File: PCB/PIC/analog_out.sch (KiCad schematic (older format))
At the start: 27 parts, among them J19 TB_1X2, Q1 PBSS5240XF, Q14 BC817-40, U18 LM358, U21 MCP6022

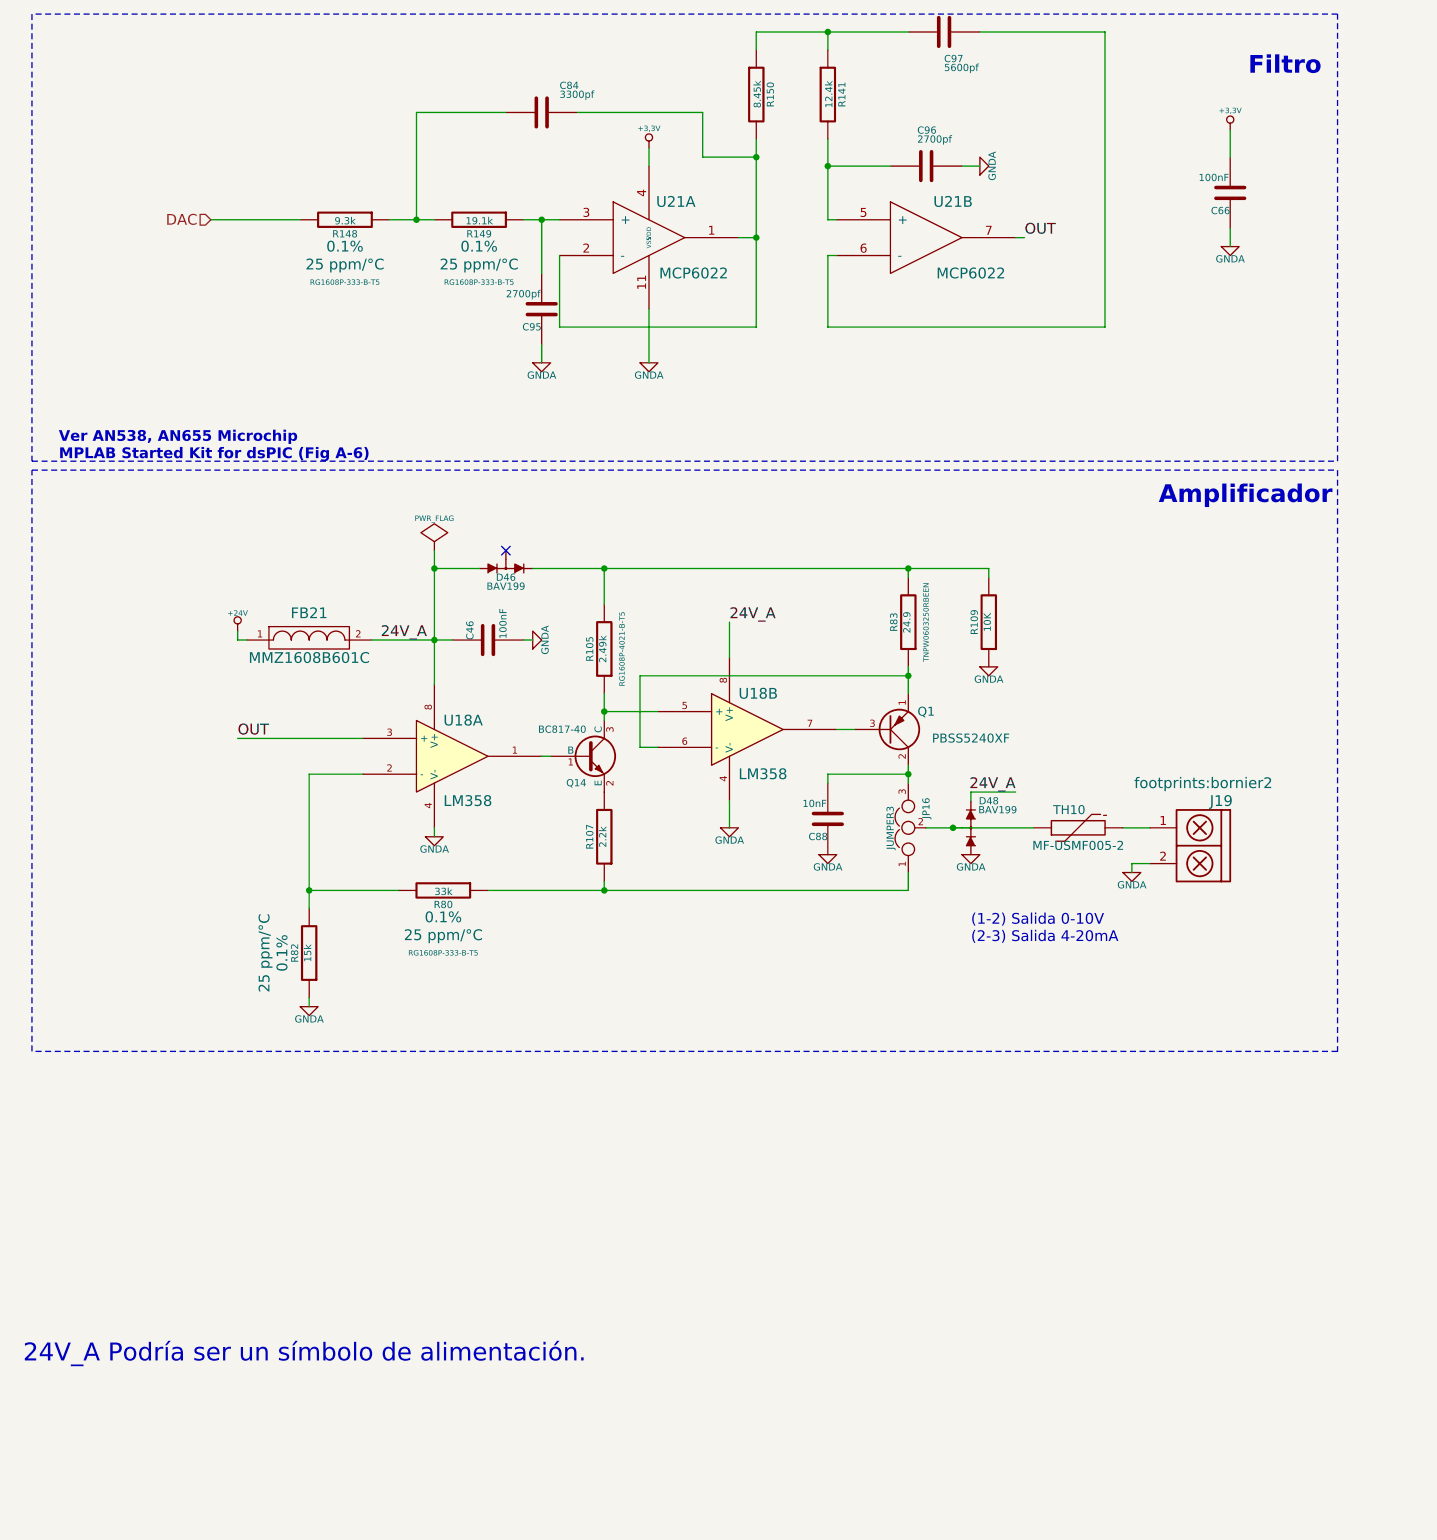
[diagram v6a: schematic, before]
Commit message: rev02 se completa campo num. de frabicante(manf#) CIAA-PIC
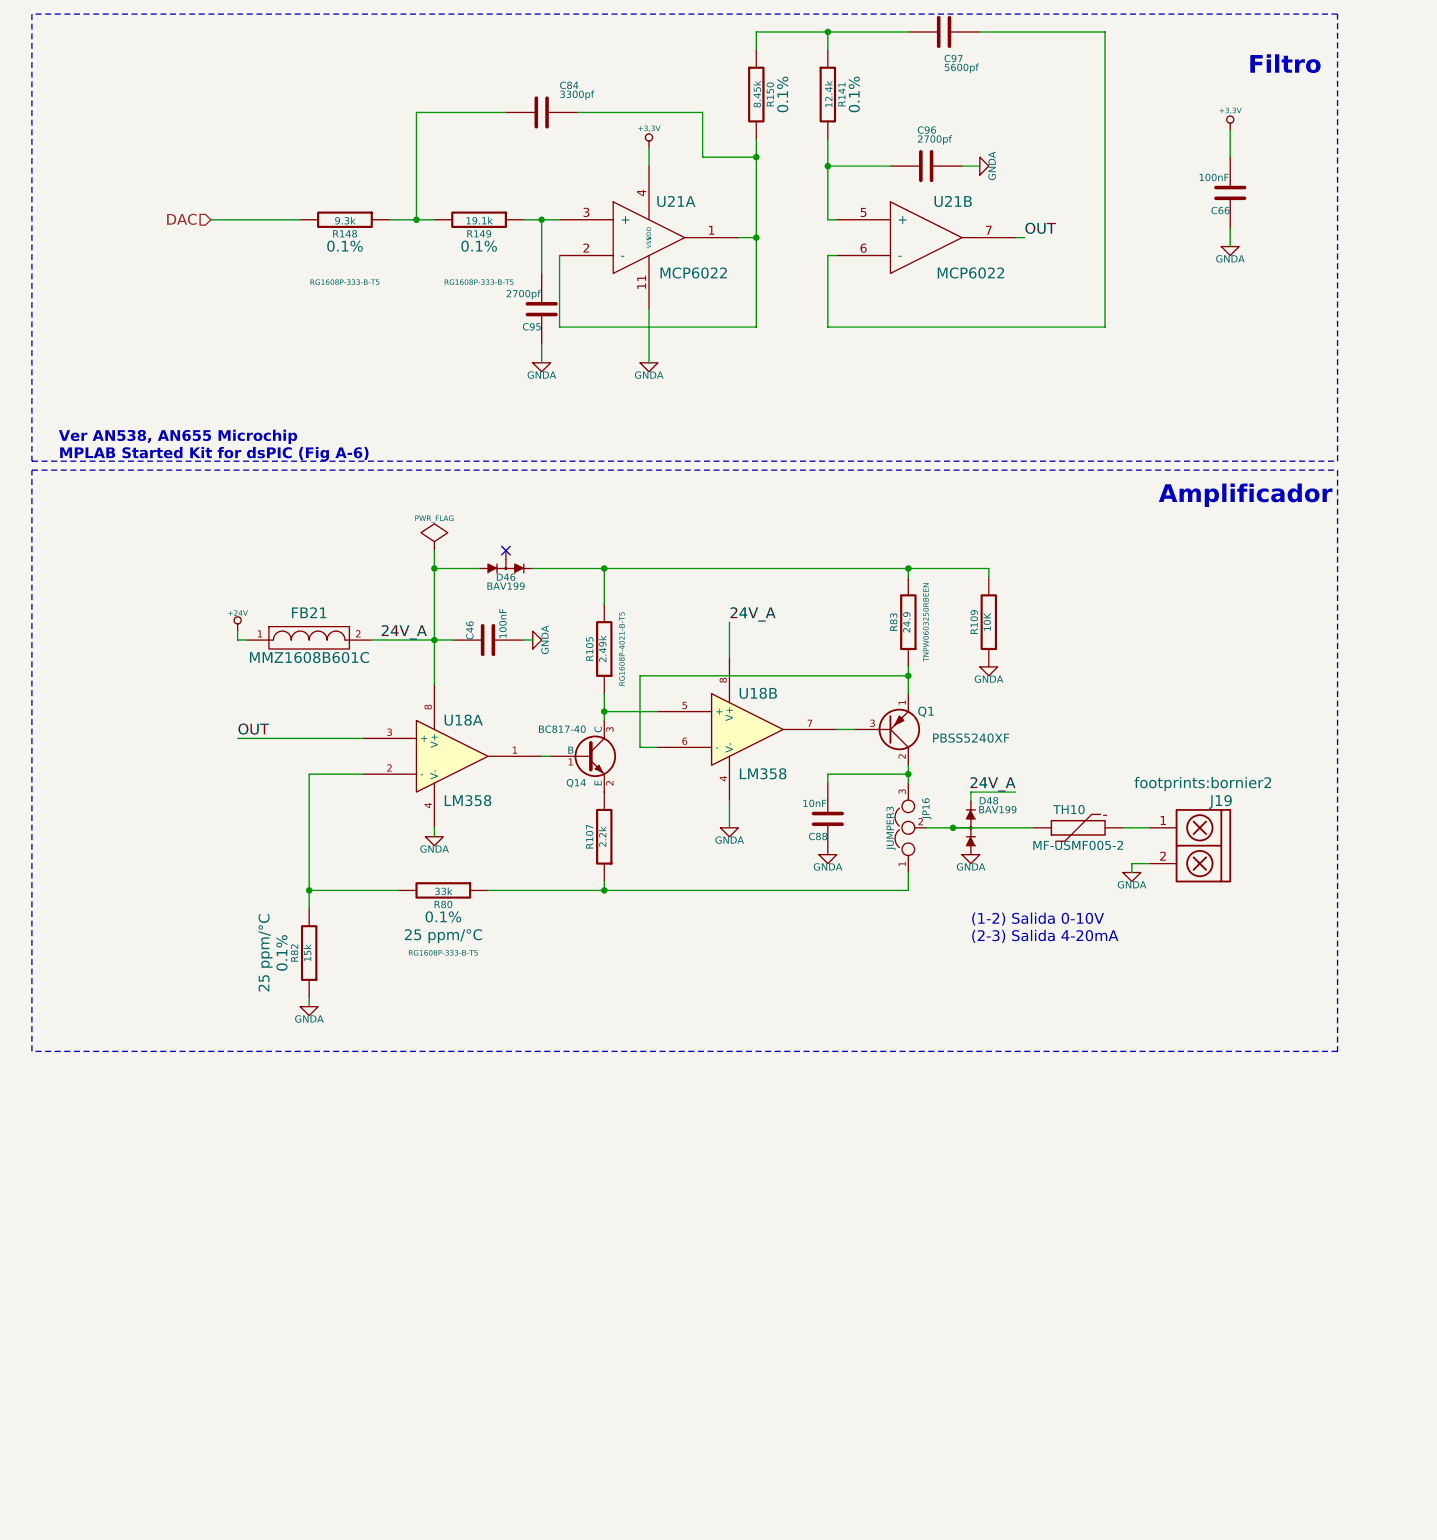
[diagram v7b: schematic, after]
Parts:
- C46, C66: #manf C0603C104K5RACTU -> (none); manf# (none) -> C0603C104K5RACTU
- C84: manf# (none) -> GRM033R71E331KA01D
- C88: #manf C0603C103K5RACTU -> (none); manf# (none) -> C0603C103K5RACTU
- C95, C96: manf# (none) -> CL10B272KB8SFNC
- C97: manf# (none) -> CL10B562KB8SFNC
- D46, D48: #manf BAV199LT1G -> (none); manf# (none) -> BAV199LT1G
- FB21: #manf MMZ1608B601CTAH0 -> (none); manf# (none) -> MMZ1608B601CTAH0
- J19: #manf OSTTC022162 -> (none); manf# (none) -> OSTTC022162
- Q1: #manf PBSS5240XF -> (none); manf# (none) -> PBSS5240XF
- Q14: #manf BC817-40LT3G -> (none); manf# (none) -> BC817-40LT3G
- R105, R83: #manf ERA-3AEB2491V -> (none); manf# (none) -> ERA-3AEB2491V
- R107: #manf ERJ-8GEYJ222V -> (none); manf# (none) -> ERJ-8GEYJ222V
- R109: #manf RC0603JR-0710KL -> (none); manf# (none) -> RC0603JR-0710KL
- R141: manf# (none) -> RC0603FR-0712K4L; tol (none) -> 0.1%
- R148: TC 25 ppm/°C -> (none); manf# (none) -> RC0603FR-079K31L
- R149: TC 25 ppm/°C -> (none); manf# (none) -> RC0603FR-0719K1L
- R150: manf# (none) -> ERJ-3EKF8451V; tol (none) -> 0.1%
- R80: #manf ERA-3AEB333V -> (none); manf# (none) -> ERA-3AEB333V
- R82: #manf RG1608P-153-B-T5 -> (none); manf# (none) -> RG1608P-153-B-T5
- TH10: #manf MF-USMF005-2 -> (none); manf# (none) -> MF-USMF005-2
- U18: #manf LM358DG -> (none); manf# (none) -> LM358DG
- U21: footprint (none) -> footprints:-SOIC8; manf# (none) -> MCP6022T-I/SN
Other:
- note removed: "24V_A Podría ser un símbolo de alimentación."
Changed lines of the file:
@@
 F 2 "Capacitors_SMD:C_0603" H 5038 4050 30  0001 C CNN
 F 3 "~" H 5000 4200 60  0000 C CNN
-F 4 "C0603C104K5RACTU" H 5000 4200 60  0001 C CNN "#manf"
+F 4 "C0603C104K5RACTU" H 5000 4200 60  0001 C CNN "manf#"
 	1    5000 4200
 	0    -1   -1   0
@@
 F 4 "0.1%" V 4900 5600 60  0000 C CNN "Tol"
 F 5 "25 ppm/°C" V 5000 5600 60  0000 C CNN "TC"
-F 6 "ERA-3AEB333V" V 4750 5600 60  0001 C CNN "#manf"
+F 6 "ERA-3AEB333V" V 4750 5600 60  0001 C CNN "manf#"
 	1    4750 5600
 	0    1    1    0
@@
 F 4 "0.1%" V 4150 5950 60  0000 C CNN "Tol"
 F 5 "25 ppm/°C" V 4250 5950 60  0000 C CNN "TC"
-F 6 "RG1608P-153-B-T5" V 4000 5950 60  0001 C CNN "#manf"
+F 6 "RG1608P-153-B-T5" V 4000 5950 60  0001 C CNN "manf#"
 	1    4000 5950
 	-1   0    0    1
@@
 F 2 "SMD_Packages:SOIC-8-N" H 4800 4850 60  0001 C CNN
 F 3 "" H 4800 4850 60  0000 C CNN
-F 4 "LM358DG " H 4800 4850 60  0001 C CNN "#manf"
+F 4 "LM358DG " H 4800 4850 60  0001 C CNN "manf#"
 	1    4800 4850
 	1    0    0    -1
@@
 F 2 "footprints:bornier2" H 9100 5700 60  0000 C CNN
 F 3 "~" H 9000 5400 60  0000 C CNN
-F 4 "OSTTC022162" H 9050 5350 60  0001 C CNN "#manf"
+F 4 "OSTTC022162" H 9050 5350 60  0001 C CNN "manf#"
 	1    9050 5350
 	-1   0    0    -1
@@
 F 2 "footprints:SM0603" H 4000 4200 60  0001 C CNN
 F 3 "~" H 4000 4200 60  0000 C CNN
-F 4 "MMZ1608B601CTAH0" H 4000 4200 60  0001 C CNN "#manf"
+F 4 "MMZ1608B601CTAH0" H 4000 4200 60  0001 C CNN "manf#"
 	1    4000 4200
 	1    0    0    -1
@@
 F 2 "footprints:SOT23" H 5350 4952 29  0001 C CNN
 F 3 "~" H 5550 4850 60  0000 C CNN
-F 4 "BC817-40LT3G" H 5550 4850 60  0001 C CNN "#manf"
+F 4 "BC817-40LT3G" H 5550 4850 60  0001 C CNN "manf#"
 	1    5550 4850
 	1    0    0    -1
@@
 F 2 "Resistors_SMD:R_1206" V 5580 5300 30  0001 C CNN
 F 3 "~" H 5650 5300 30  0000 C CNN
-F 4 "ERJ-8GEYJ222V " V 5650 5300 60  0001 C CNN "#manf"
+F 4 "ERJ-8GEYJ222V " V 5650 5300 60  0001 C CNN "manf#"
 	1    5650 5300
 	-1   0    0    1
@@
 F 2 "Resistors_SMD:R_0603" V 5580 4250 30  0001 C CNN
 F 3 "RG1608P-4021-B-T5" V 5550 4250 30  0000 C CNN
-F 4 "ERA-3AEB2491V " V 5650 4250 60  0001 C CNN "#manf"
+F 4 "ERA-3AEB2491V " V 5650 4250 60  0001 C CNN "manf#"
 	1    5650 4250
 	-1   0    0    1
@@
 F 2 "Resistors_SMD:R_0603" V 7280 4100 30  0001 C CNN
 F 3 "TNPW0603250RBEEN" V 7250 4100 30  0000 C CNN
-F 4 "ERA-3AEB2491V " V 7350 4100 60  0001 C CNN "#manf"
+F 4 "ERA-3AEB2491V " V 7350 4100 60  0001 C CNN "manf#"
 	1    7350 4100
 	-1   0    0    1
@@
 F 2 "Resistors_SMD:R_0603" V 7730 4100 30  0001 C CNN
 F 3 "~" H 7800 4100 30  0000 C CNN
-F 4 "RC0603JR-0710KL" V 7800 4100 60  0001 C CNN "#manf"
+F 4 "RC0603JR-0710KL" V 7800 4100 60  0001 C CNN "manf#"
 	1    7800 4100
 	-1   0    0    1
@@
 F 2 "footprints:-SOT89" H 7700 5250 60  0001 C CNN
 F 3 "" H 7700 5250 60  0000 C CNN
-F 4 "BAV199LT1G " V 7700 5250 60  0001 C CNN "#manf"
+F 4 "BAV199LT1G " V 7700 5250 60  0001 C CNN "manf#"
 	1    7700 5250
 	0    -1   -1   0
@@
 F 2 "Capacitors_SMD:C_0603" H 6938 5050 30  0001 C CNN
 F 3 "~" H 6900 5200 60  0000 C CNN
-F 4 "C0603C103K5RACTU " H 6900 5200 60  0001 C CNN "#manf"
+F 4 "C0603C103K5RACTU " H 6900 5200 60  0001 C CNN "manf#"
 	1    6900 5200
 	-1   0    0    1
@@
 F 2 "footprints:SOT23-DIODE" H 5100 3800 60  0001 C CNN
 F 3 "" H 5100 3800 60  0000 C CNN
-F 4 "BAV199LT1G " H 5100 3800 60  0001 C CNN "#manf"
+F 4 "BAV199LT1G " H 5100 3800 60  0001 C CNN "manf#"
 	1    5100 3800
 	1    0    0    -1
@@
 F 2 "footprints:MF-USMF" H 8300 5250 60  0001 C CNN
 F 3 "~" H 8300 5250 60  0000 C CNN
-F 4 "MF-USMF005-2" V 8300 5250 60  0001 C CNN "#manf"
+F 4 "MF-USMF005-2" V 8300 5250 60  0001 C CNN "manf#"
 	1    8300 5250
 	0    -1   -1   0
@@
 F 2 "footprints:-SOT89" H 7650 4650 60  0001 C CNN
 F 3 "~" H 7250 4700 60  0000 C CNN
-F 4 "PBSS5240XF" H 7250 4700 60  0001 C CNN "#manf"
+F 4 "PBSS5240XF" H 7250 4700 60  0001 C CNN "manf#"
 	1    7250 4700
 	1    0    0    1
@@
 F 2 "Resistors_SMD:R_0603" V 6830 1150 30  0001 C CNN
 F 3 "~" H 6900 1150 30  0000 C CNN
+F 4 "RC0603FR-0712K4L" V 6900 1150 60  0001 C CNN "manf#"
+F 5 "0.1%" V 7050 1150 60  0000 C CNN "tol"
 	1    6900 1150
 	1    0    0    -1
@@
 F 2 "Capacitors_SMD:C_0603" H 9188 1550 30  0001 C CNN
 F 3 "~" H 9150 1700 60  0000 C CNN
-F 4 "C0603C104K5RACTU" H 9150 1700 60  0001 C CNN "#manf"
+F 4 "C0603C104K5RACTU" H 9150 1700 60  0001 C CNN "manf#"
 	1    9150 1700
 	-1   0    0    1
@@
 F 3 "RG1608P-333-B-T5" V 5300 1850 30  0000 C CNN
 F 4 "0.1%" V 5100 1850 60  0000 C CNN "Tol"
-F 5 "25 ppm/°C" V 5200 1850 60  0000 C CNN "TC"
+F 5 "RC0603FR-0719K1L" V 4950 1850 60  0001 C CNN "manf#"
 	1    4950 1850
 	0    1    1    0
@@
 F 3 "RG1608P-333-B-T5" V 4550 1850 30  0000 C CNN
 F 4 "0.1%" V 4350 1850 60  0000 C CNN "Tol"
-F 5 "25 ppm/°C" V 4450 1850 60  0000 C CNN "TC"
+F 5 "RC0603FR-079K31L" V 4200 1850 60  0001 C CNN "manf#"
 	1    4200 1850
 	0    1    1    0
@@
 F 2 "" H 5338 2200 30  0001 C CNN
 F 3 "~" H 5300 2350 60  0000 C CNN
+F 4 "CL10B272KB8SFNC" H 5300 2350 60  0001 C CNN "manf#"
 	1    5300 2350
 	-1   0    0    1
@@
 F 2 "Resistors_SMD:R_0603" V 6430 1150 30  0001 C CNN
 F 3 "~" H 6500 1150 30  0000 C CNN
+F 4 "ERJ-3EKF8451V " V 6500 1150 60  0001 C CNN "manf#"
+F 5 "0.1%" V 6650 1150 60  0000 C CNN "tol"
 	1    6500 1150
 	1    0    0    -1
@@
 F 2 "" H 7588 650 30  0001 C CNN
 F 3 "~" H 7550 800 60  0000 C CNN
+F 4 "CL10B562KB8SFNC " V 7550 800 60  0001 C CNN "manf#"
 	1    7550 800
 	0    1    1    0
@@
 F 2 "" H 7488 1400 30  0001 C CNN
 F 3 "~" H 7450 1550 60  0000 C CNN
+F 4 "CL10B272KB8SFNC" V 7450 1550 60  0001 C CNN "manf#"
 	1    7450 1550
 	0    1    1    0
@@
 F 0 "U21" H 7600 2150 60  0000 C CNN
 F 1 "MCP6022" H 7700 1750 60  0000 C CNN
-F 2 "" H 7450 1950 60  0001 C CNN
+F 2 "footprints:-SOIC8" H 7450 1950 60  0001 C CNN
 F 3 "~" H 7450 1950 60  0000 C CNN
+F 4 "MCP6022T-I/SN" H 7450 1950 60  0001 C CNN "manf#"
 	2    7450 1950
 	1    0    0    -1
@@
 F 2 "Capacitors_SMD:C_0603" H 5338 1100 30  0001 C CNN
 F 3 "~" H 5300 1250 60  0000 C CNN
+F 4 "GRM033R71E331KA01D" V 5300 1250 60  0001 C CNN "manf#"
 	1    5300 1250
 	0    1    1    0
@@
 Wire Wire Line
 	6900 1400 6900 1850
-Text Notes 2400 8250 0    100  ~ 0
-24V_A Podría ser un símbolo de alimentación.
 Text Notes 9250 1050 0    99   ~ 20
 Filtro\n
